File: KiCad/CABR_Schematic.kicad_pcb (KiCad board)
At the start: 2 copper layers, 23.5 x 59.1 mm, 20 parts, among them J1 Screw_Terminal_01x02, J2 0.1" Header, J3 Program Header, J4 MicroSwitch, J5 Screw_Terminal_01x02, Q1 PBSS4250X, U1 AZ1117-5.0, U2 ATtiny85-20SU

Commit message: updated PCB again
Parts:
- moved J5 3.94 mm to (145.3, 107.2)
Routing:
- net GND: track 112.9 -> 120.5 mm
- net Net-(C2-Pad1): track 57.5 -> 56.5 mm
- net Net-(C1-Pad1): track 63.1 -> 62.5 mm
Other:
- board size 23.5 x 59.1 mm -> 23.5 x 54.6 mm
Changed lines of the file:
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@@
     (thickness 1.6)
     (drawings 9)
-    (tracks 194)
+    (tracks 200)
     (zones 0)
     (modules 20)
@@
       (drillshape 0)
       (scaleselection 1)
-      (outputdirectory "C:/Users/chandler.lofland/OtherProjects/CABR/KiCad/Gerber/"))
+      (outputdirectory "G:/Projects/3D Printing/CABR/KiCad/Gerber/"))
   )
   (net 0 "")
@@
   )
   (module XT60:XT60 (layer F.Cu)
-    (at 145.415 111.125)
+    (at 145.288 107.188)
     (fp_text reference J5 (at 3.556 6.096) (layer F.SilkS)
       (effects (font (size 1 1) (thickness 0.15)))
@@
     )
   )
-  (gr_text Power (at 153.67 116.84) (layer F.SilkS)
+  (gr_text Power (at 154.432 112.776) (layer F.SilkS)
     (effects (font (size 1 1) (thickness 0.15)))
   )
-  (gr_line (start 160.655 118.745) (end 160.655 112.395) (layer Edge.Cuts) (width 0.05))
-  (gr_line (start 137.16 118.745) (end 160.655 118.745) (layer Edge.Cuts) (width 0.05))
-  (gr_line (start 137.16 112.395) (end 137.16 118.745) (layer Edge.Cuts) (width 0.05))
+  (gr_line (start 160.655 114.3) (end 160.655 112.395) (layer Edge.Cuts) (width 0.05))
+  (gr_line (start 137.16 114.3) (end 160.655 114.3) (layer Edge.Cuts) (width 0.05))
+  (gr_line (start 137.16 112.395) (end 137.16 114.3) (layer Edge.Cuts) (width 0.05))
   (gr_line (start 137.16 59.69) (end 137.16 63.5) (layer Edge.Cuts) (width 0.05))
   (gr_line (start 160.655 59.69) (end 137.16 59.69) (layer Edge.Cuts) (width 0.05))
@@
   (gr_line (start 160.655 112.395) (end 160.655 63.5) (layer Edge.Cuts) (width 0.05))
   (gr_line (start 137.16 63.5) (end 137.16 112.395) (layer Edge.Cuts) (width 0.05))
-  (segment (start 157.48 69.469) (end 153.035 65.024) (width 0.5) (layer F.Cu) (net 1))
-  (segment (start 157.48 74.55) (end 157.48 69.469) (width 0.5) (layer F.Cu) (net 1))
+  (segment (start 157.48 69.469) (end 153.035 65.024) (width 1) (layer F.Cu) (net 1))
+  (segment (start 157.48 74.55) (end 157.48 69.469) (width 1) (layer F.Cu) (net 1))
   (via (at 157.48 76.2) (size 0.8) (drill 0.4) (layers F.Cu B.Cu) (net 1))
-  (segment (start 157.48 91.44) (end 148.844 100.076) (width 0.5) (layer B.Cu) (net 1))
-  (segment (start 157.48 76.2) (end 157.48 91.44) (width 0.5) (layer B.Cu) (net 1))
-  (segment (start 157.48 74.55) (end 157.48 76.2) (width 0.5) (layer F.Cu) (net 1))
+  (segment (start 157.48 91.44) (end 148.844 100.076) (width 1) (layer B.Cu) (net 1))
+  (segment (start 157.48 76.2) (end 157.48 91.44) (width 1) (layer B.Cu) (net 1))
+  (segment (start 157.48 74.55) (end 157.48 76.2) (width 1) (layer F.Cu) (net 1))
   (via (at 148.844 100.076) (size 0.8) (drill 0.4) (layers F.Cu B.Cu) (net 1))
   (segment (start 146.089 100.076) (end 146.075 100.09) (width 0.5) (layer F.Cu) (net 1))
-  (segment (start 156.337 70.612) (end 157.48 69.469) (width 0.5) (layer F.Cu) (net 1))
-  (segment (start 154.304 70.612) (end 156.337 70.612) (width 0.5) (layer F.Cu) (net 1))
+  (segment (start 156.337 70.612) (end 157.48 69.469) (width 1) (layer F.Cu) (net 1))
+  (segment (start 154.304 70.612) (end 156.337 70.612) (width 1) (layer F.Cu) (net 1))
   (segment (start 145.6595 100.5055) (end 146.075 100.09) (width 0.25) (layer F.Cu) (net 1))
   (segment (start 143.256 100.5055) (end 145.6595 100.5055) (width 0.25) (layer F.Cu) (net 1))
-  (segment (start 145.415 102.6645) (end 143.256 100.5055) (width 0.5) (layer F.Cu) (net 1))
-  (segment (start 145.415 111.125) (end 145.415 102.6645) (width 0.5) (layer F.Cu) (net 1))
-  (segment (start 146.2555 102.6645) (end 148.844 100.076) (width 0.5) (layer F.Cu) (net 1))
-  (segment (start 145.415 102.6645) (end 146.2555 102.6645) (width 0.5) (layer F.Cu) (net 1))
+  (segment (start 146.2555 102.6645) (end 148.844 100.076) (width 1) (layer F.Cu) (net 1))
+  (segment (start 145.415 102.6645) (end 146.2555 102.6645) (width 1) (layer F.Cu) (net 1))
+  (segment (start 145.288 102.5375) (end 144.81925 102.06875) (width 0.25) (layer F.Cu) (net 1))
+  (segment (start 145.415 102.6645) (end 144.81925 102.06875) (width 1) (layer F.Cu) (net 1))
+  (segment (start 144.81925 102.06875) (end 143.256 100.5055) (width 1) (layer F.Cu) (net 1))
+  (segment (start 145.288 107.188) (end 145.288 106.68) (width 1) (layer F.Cu) (net 1))
+  (segment (start 147.828 104.14) (end 146.3525 102.6645) (width 1) (layer F.Cu) (net 1))
+  (segment (start 146.3525 102.6645) (end 145.415 102.6645) (width 1) (layer F.Cu) (net 1))
+  (segment (start 145.288 106.68) (end 147.828 104.14) (width 1) (layer F.Cu) (net 1))
   (segment (start 144.2075 95.49) (end 146.075 95.49) (width 0.25) (layer F.Cu) (net 2))
   (segment (start 143.256 96.4415) (end 144.2075 95.49) (width 0.25) (layer F.Cu) (net 2))
@@
   (segment (start 145.542 86.614) (end 145.542 84.488) (width 0.25) (layer F.Cu) (net 2))
   (via (at 150.876 72.39) (size 0.8) (drill 0.4) (layers F.Cu B.Cu) (net 2))
-  (segment (start 143.002 72.39) (end 138.938 76.454) (width 0.5) (layer B.Cu) (net 2))
-  (segment (start 150.876 72.39) (end 143.002 72.39) (width 0.5) (layer B.Cu) (net 2))
-  (segment (start 138.938 76.454) (end 138.938 98.355002) (width 0.5) (layer B.Cu) (net 2))
-  (segment (start 138.938 98.355002) (end 148.707999 108.125001) (width 0.5) (layer B.Cu) (net 2))
-  (segment (start 148.707999 108.125001) (end 149.915001 108.125001) (width 0.5) (layer B.Cu) (net 2))
-  (segment (start 149.915001 108.125001) (end 152.915 111.125) (width 0.5) (layer B.Cu) (net 2))
+  (segment (start 143.002 72.39) (end 138.938 76.454) (width 1) (layer B.Cu) (net 2))
+  (segment (start 150.876 72.39) (end 143.002 72.39) (width 1) (layer B.Cu) (net 2))
+  (segment (start 138.938 76.454) (end 138.938 98.355002) (width 1) (layer B.Cu) (net 2))
   (segment (start 150.92 72.434) (end 150.876 72.39) (width 0.5) (layer F.Cu) (net 2))
-  (segment (start 150.92 74.065) (end 150.92 72.434) (width 0.5) (layer F.Cu) (net 2))
+  (segment (start 150.92 74.065) (end 150.92 72.434) (width 1) (layer F.Cu) (net 2))
   (segment (start 143.256 98.6305) (end 143.256 96.4415) (width 0.25) (layer F.Cu) (net 2))
   (via (at 140.716 98.044) (size 0.8) (drill 0.4) (layers F.Cu B.Cu) (net 2))
@@
   (segment (start 156.8935 97.028) (end 156.8935 92.456) (width 0.25) (layer F.Cu) (net 2))
   (segment (start 155.194 98.7275) (end 156.8935 97.028) (width 0.25) (layer F.Cu) (net 2))
+  (segment (start 138.938 107.95) (end 138.938 98.355002) (width 1) (layer B.Cu) (net 2))
+  (segment (start 148.216 111.76) (end 142.748 111.76) (width 1) (layer B.Cu) (net 2))
+  (segment (start 152.788 107.188) (end 148.216 111.76) (width 1) (layer B.Cu) (net 2))
+  (segment (start 142.748 111.76) (end 138.938 107.95) (width 1) (layer B.Cu) (net 2))
   (segment (start 141.605 86.825) (end 141.605 85.725) (width 0.25) (layer F.Cu) (net 3))
   (segment (start 144.409999 89.629999) (end 141.605 86.825) (width 0.25) (layer F.Cu) (net 3))
   (segment (start 148.049999 89.629999) (end 144.409999 89.629999) (width 0.25) (layer F.Cu) (net 3))
   (segment (start 149.225 90.805) (end 148.049999 89.629999) (width 0.25) (layer F.Cu) (net 3))
-  (segment (start 140.505 85.725) (end 138.43 83.65) (width 0.25) (layer F.Cu) (net 3))
-  (segment (start 141.605 85.725) (end 140.505 85.725) (width 0.25) (layer F.Cu) (net 3))
-  (segment (start 138.43 83.65) (end 138.43 78.74) (width 0.25) (layer F.Cu) (net 3))
-  (segment (start 139.954 77.216) (end 141.224 77.216) (width 0.25) (layer F.Cu) (net 3))
-  (segment (start 138.43 78.74) (end 139.954 77.216) (width 0.25) (layer F.Cu) (net 3))
   (segment (start 152.375 97.79) (end 146.075 97.79) (width 0.25) (layer F.Cu) (net 3))
   (via (at 156.718 82.46) (size 0.8) (drill 0.4) (layers F.Cu B.Cu) (net 3))
@@
   (segment (start 155.194 96.8525) (end 155.194 95.504) (width 0.25) (layer F.Cu) (net 3))
   (segment (start 155.194 95.504) (end 154.686 94.996) (width 0.25) (layer F.Cu) (net 3))
+  (segment (start 139.954 77.216) (end 141.224 77.216) (width 0.25) (layer F.Cu) (net 3))
+  (segment (start 139.7 77.47) (end 139.954 77.216) (width 0.25) (layer F.Cu) (net 3))
+  (segment (start 139.7 84.92) (end 139.7 77.47) (width 0.25) (layer F.Cu) (net 3))
+  (segment (start 141.605 85.725) (end 140.505 85.725) (width 0.25) (layer F.Cu) (net 3))
+  (segment (start 140.505 85.725) (end 139.7 84.92) (width 0.25) (layer F.Cu) (net 3))
   (segment (start 143.256 93.315) (end 143.256 94.5665) (width 0.25) (layer F.Cu) (net 4))
   (segment (start 142.24 92.299) (end 143.256 93.315) (width 0.25) (layer F.Cu) (net 4))
@@
   (segment (start 145.161 83.185) (end 145.575 83.185) (width 0.25) (layer F.Cu) (net 5))
   (segment (start 144.018 84.328) (end 145.161 83.185) (width 0.25) (layer F.Cu) (net 5))
-  (segment (start 145.535 65.024) (end 149.352 68.841) (width 0.5) (layer F.Cu) (net 6))
-  (segment (start 149.352 68.841) (end 149.352 74.2505) (width 0.5) (layer F.Cu) (net 6))
-  (segment (start 149.352 74.2505) (end 150.6665 75.565) (width 0.5) (layer F.Cu) (net 6))
+  (segment (start 145.535 65.024) (end 149.352 68.841) (width 1) (layer F.Cu) (net 6))
+  (segment (start 149.352 68.841) (end 149.352 74.2505) (width 1) (layer F.Cu) (net 6))
+  (segment (start 149.352 74.2505) (end 150.6665 75.565) (width 1) (layer F.Cu) (net 6))
   (segment (start 150.6665 75.565) (end 151.0665 75.565) (width 0.5) (layer F.Cu) (net 6))
   (segment (start 155.067 75.587) (end 155.067 75.565) (width 0.5) (layer F.Cu) (net 6))
   (segment (start 151.0665 75.565) (end 155.067 75.565) (width 0.25) (layer F.Cu) (net 6))
   (segment (start 151.004 70.462) (end 151.004 70.612) (width 0.25) (layer F.Cu) (net 6))
-  (segment (start 149.383 68.841) (end 151.004 70.462) (width 0.5) (layer F.Cu) (net 6))
+  (segment (start 149.383 68.841) (end 151.004 70.462) (width 1) (layer F.Cu) (net 6))
   (segment (start 149.352 68.841) (end 149.383 68.841) (width 0.25) (layer F.Cu) (net 6))
   (via (at 151.13 85.725) (size 0.8) (drill 0.4) (layers F.Cu B.Cu) (net 7))

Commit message: edited step file
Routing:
- net Net-(C2-Pad1): track 56.5 -> 58.0 mm
- net Net-(J4-Pad2): track 26.7 -> 27.9 mm
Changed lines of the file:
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@@
     (thickness 1.6)
     (drawings 9)
-    (tracks 200)
+    (tracks 199)
     (zones 0)
     (modules 20)
@@
   (segment (start 156.8935 92.456) (end 158.242 91.1075) (width 0.25) (layer F.Cu) (net 2))
   (via (at 147.315347 84.840653) (size 0.8) (drill 0.4) (layers F.Cu B.Cu) (net 2))
-  (segment (start 146.075 91.415) (end 146.685 90.805) (width 0.25) (layer F.Cu) (net 2))
-  (segment (start 146.075 95.49) (end 146.075 91.415) (width 0.25) (layer F.Cu) (net 2))
   (via (at 144.272 90.678) (size 0.8) (drill 0.4) (layers F.Cu B.Cu) (net 2))
   (segment (start 146.685 90.805) (end 144.399 90.805) (width 0.25) (layer F.Cu) (net 2))
@@
   (segment (start 138.938 98.355002) (end 139.249002 98.044) (width 0.25) (layer B.Cu) (net 2))
   (segment (start 141.281685 98.044) (end 140.716 98.044) (width 0.25) (layer F.Cu) (net 2))
-  (segment (start 156.8935 97.028) (end 156.8935 92.456) (width 0.25) (layer F.Cu) (net 2))
-  (segment (start 155.194 98.7275) (end 156.8935 97.028) (width 0.25) (layer F.Cu) (net 2))
   (segment (start 138.938 107.95) (end 138.938 98.355002) (width 1) (layer B.Cu) (net 2))
   (segment (start 148.216 111.76) (end 142.748 111.76) (width 1) (layer B.Cu) (net 2))
   (segment (start 152.788 107.188) (end 148.216 111.76) (width 1) (layer B.Cu) (net 2))
   (segment (start 142.748 111.76) (end 138.938 107.95) (width 1) (layer B.Cu) (net 2))
+  (segment (start 146.685 92.964) (end 146.685 90.805) (width 0.25) (layer F.Cu) (net 2))
+  (segment (start 146.685 93.218) (end 146.685 92.964) (width 0.25) (layer F.Cu) (net 2))
+  (segment (start 146.075 95.49) (end 146.075 93.828) (width 0.25) (layer F.Cu) (net 2))
+  (segment (start 146.075 93.828) (end 146.685 93.218) (width 0.25) (layer F.Cu) (net 2))
+  (segment (start 155.194 98.7275) (end 157.449737 96.471763) (width 0.25) (layer F.Cu) (net 2))
+  (segment (start 157.449737 96.471763) (end 157.449737 93.012237) (width 0.25) (layer F.Cu) (net 2))
+  (segment (start 157.449737 93.012237) (end 156.8935 92.456) (width 0.25) (layer F.Cu) (net 2))
   (segment (start 141.605 86.825) (end 141.605 85.725) (width 0.25) (layer F.Cu) (net 3))
   (segment (start 144.409999 89.629999) (end 141.605 86.825) (width 0.25) (layer F.Cu) (net 3))
@@
   (segment (start 149.225 90.805) (end 148.049999 89.629999) (width 0.25) (layer F.Cu) (net 3))
   (segment (start 152.375 97.79) (end 146.075 97.79) (width 0.25) (layer F.Cu) (net 3))
-  (via (at 156.718 82.46) (size 0.8) (drill 0.4) (layers F.Cu B.Cu) (net 3))
-  (segment (start 156.318001 82.859999) (end 156.318001 86.505999) (width 0.25) (layer B.Cu) (net 3))
-  (segment (start 156.718 82.46) (end 156.318001 82.859999) (width 0.25) (layer B.Cu) (net 3))
-  (via (at 153.416 89.408) (size 0.8) (drill 0.4) (layers F.Cu B.Cu) (net 3))
-  (segment (start 156.318001 86.505999) (end 153.416 89.408) (width 0.25) (layer B.Cu) (net 3))
-  (segment (start 150.074999 89.955001) (end 149.225 90.805) (width 0.25) (layer F.Cu) (net 3))
-  (segment (start 150.400001 89.629999) (end 150.074999 89.955001) (width 0.25) (layer F.Cu) (net 3))
-  (segment (start 152.628316 89.629999) (end 150.400001 89.629999) (width 0.25) (layer F.Cu) (net 3))
-  (segment (start 152.850315 89.408) (end 152.628316 89.629999) (width 0.25) (layer F.Cu) (net 3))
-  (segment (start 153.416 89.408) (end 152.850315 89.408) (width 0.25) (layer F.Cu) (net 3))
-  (segment (start 156.628 82.55) (end 156.718 82.46) (width 0.25) (layer F.Cu) (net 3))
-  (segment (start 157.226 82.55) (end 156.628 82.55) (width 0.25) (layer F.Cu) (net 3))
-  (segment (start 157.7825 81.28) (end 157.7825 81.9935) (width 0.25) (layer F.Cu) (net 3))
-  (segment (start 157.7825 81.9935) (end 157.226 82.55) (width 0.25) (layer F.Cu) (net 3))
   (segment (start 154.2565 97.79) (end 155.194 96.8525) (width 0.25) (layer F.Cu) (net 3))
   (segment (start 152.375 97.79) (end 154.2565 97.79) (width 0.25) (layer F.Cu) (net 3))
+  (segment (start 139.954 77.216) (end 141.224 77.216) (width 0.25) (layer F.Cu) (net 3))
+  (segment (start 139.7 77.47) (end 139.954 77.216) (width 0.25) (layer F.Cu) (net 3))
+  (segment (start 139.7 84.92) (end 139.7 77.47) (width 0.25) (layer F.Cu) (net 3))
+  (segment (start 141.605 85.725) (end 140.505 85.725) (width 0.25) (layer F.Cu) (net 3))
+  (segment (start 140.505 85.725) (end 139.7 84.92) (width 0.25) (layer F.Cu) (net 3))
   (segment (start 149.225 92.007081) (end 149.225 90.805) (width 0.25) (layer F.Cu) (net 3))
   (segment (start 152.213919 94.996) (end 149.225 92.007081) (width 0.25) (layer F.Cu) (net 3))
@@
   (segment (start 155.194 96.8525) (end 155.194 95.504) (width 0.25) (layer F.Cu) (net 3))
   (segment (start 155.194 95.504) (end 154.686 94.996) (width 0.25) (layer F.Cu) (net 3))
-  (segment (start 139.954 77.216) (end 141.224 77.216) (width 0.25) (layer F.Cu) (net 3))
-  (segment (start 139.7 77.47) (end 139.954 77.216) (width 0.25) (layer F.Cu) (net 3))
-  (segment (start 139.7 84.92) (end 139.7 77.47) (width 0.25) (layer F.Cu) (net 3))
-  (segment (start 141.605 85.725) (end 140.505 85.725) (width 0.25) (layer F.Cu) (net 3))
-  (segment (start 140.505 85.725) (end 139.7 84.92) (width 0.25) (layer F.Cu) (net 3))
+  (via (at 159.258 82.804) (size 0.8) (drill 0.4) (layers F.Cu B.Cu) (net 3))
+  (segment (start 159.258 82.7555) (end 157.7825 81.28) (width 0.25) (layer F.Cu) (net 3))
+  (segment (start 159.258 82.804) (end 159.258 82.7555) (width 0.25) (layer F.Cu) (net 3))
+  (segment (start 159.258 82.804) (end 159.258 91.9065) (width 0.25) (layer B.Cu) (net 3))
+  (segment (start 156.568499 94.596001) (end 156.1685 94.996) (width 0.25) (layer B.Cu) (net 3))
+  (segment (start 159.258 91.9065) (end 156.568499 94.596001) (width 0.25) (layer B.Cu) (net 3))
+  (via (at 156.1685 94.996) (size 0.8) (drill 0.4) (layers F.Cu B.Cu) (net 3))
+  (segment (start 155.9145 95.25) (end 156.1685 94.996) (width 0.25) (layer F.Cu) (net 3))
+  (segment (start 155.194 95.504) (end 155.448 95.25) (width 0.25) (layer F.Cu) (net 3))
+  (segment (start 155.448 95.25) (end 155.9145 95.25) (width 0.25) (layer F.Cu) (net 3))
   (segment (start 143.256 93.315) (end 143.256 94.5665) (width 0.25) (layer F.Cu) (net 4))
   (segment (start 142.24 92.299) (end 143.256 93.315) (width 0.25) (layer F.Cu) (net 4))
@@
   (segment (start 142.875 81.915) (end 143.891 81.915) (width 0.25) (layer F.Cu) (net 11))
   (segment (start 143.891 81.915) (end 145.575 81.915) (width 0.25) (layer F.Cu) (net 11))
-  (segment (start 140.429999 88.163001) (end 145.230998 92.964) (width 0.25) (layer B.Cu) (net 11))
-  (segment (start 141.605 83.185) (end 140.429999 84.360001) (width 0.25) (layer B.Cu) (net 11))
-  (segment (start 140.429999 84.360001) (end 140.429999 88.163001) (width 0.25) (layer B.Cu) (net 11))
   (via (at 151.638 92.964) (size 0.8) (drill 0.4) (layers F.Cu B.Cu) (net 11))
-  (segment (start 145.230998 92.964) (end 151.638 92.964) (width 0.25) (layer B.Cu) (net 11))
   (segment (start 151.638 92.964) (end 153.416 92.964) (width 0.25) (layer F.Cu) (net 11))
   (segment (start 153.924 92.456) (end 155.0185 92.456) (width 0.25) (layer F.Cu) (net 11))
   (segment (start 153.416 92.964) (end 153.924 92.456) (width 0.25) (layer F.Cu) (net 11))
+  (segment (start 143.51 92.964) (end 151.638 92.964) (width 0.25) (layer B.Cu) (net 11))
+  (segment (start 140.208 89.662) (end 143.51 92.964) (width 0.25) (layer B.Cu) (net 11))
+  (segment (start 141.605 83.185) (end 140.208 84.582) (width 0.25) (layer B.Cu) (net 11))
+  (segment (start 140.208 84.582) (end 140.208 89.662) (width 0.25) (layer B.Cu) (net 11))
   (segment (start 149.92 77.065) (end 150.92 77.065) (width 0.25) (layer F.Cu) (net 12))
   (segment (start 148.2575 75.4025) (end 149.92 77.065) (width 0.25) (layer F.Cu) (net 12))

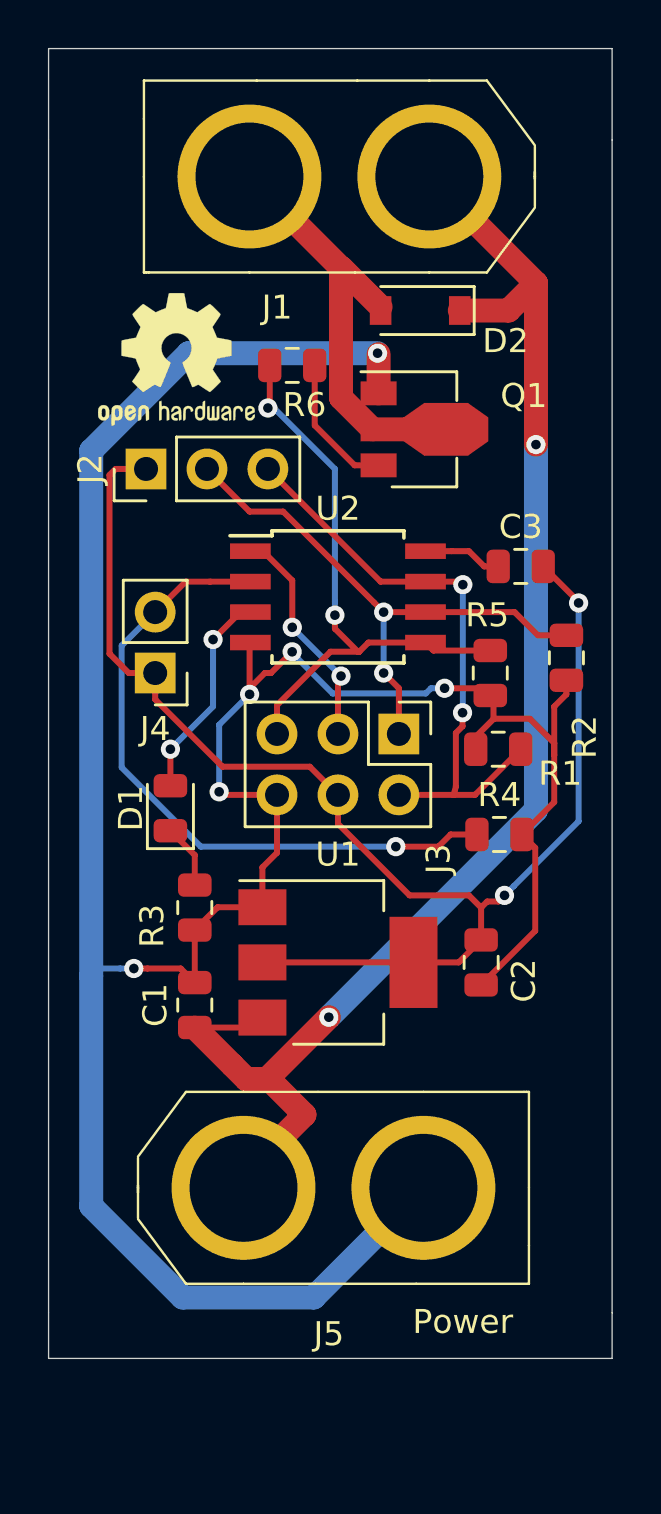
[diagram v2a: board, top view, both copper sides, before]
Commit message: fixed issue with boardfire
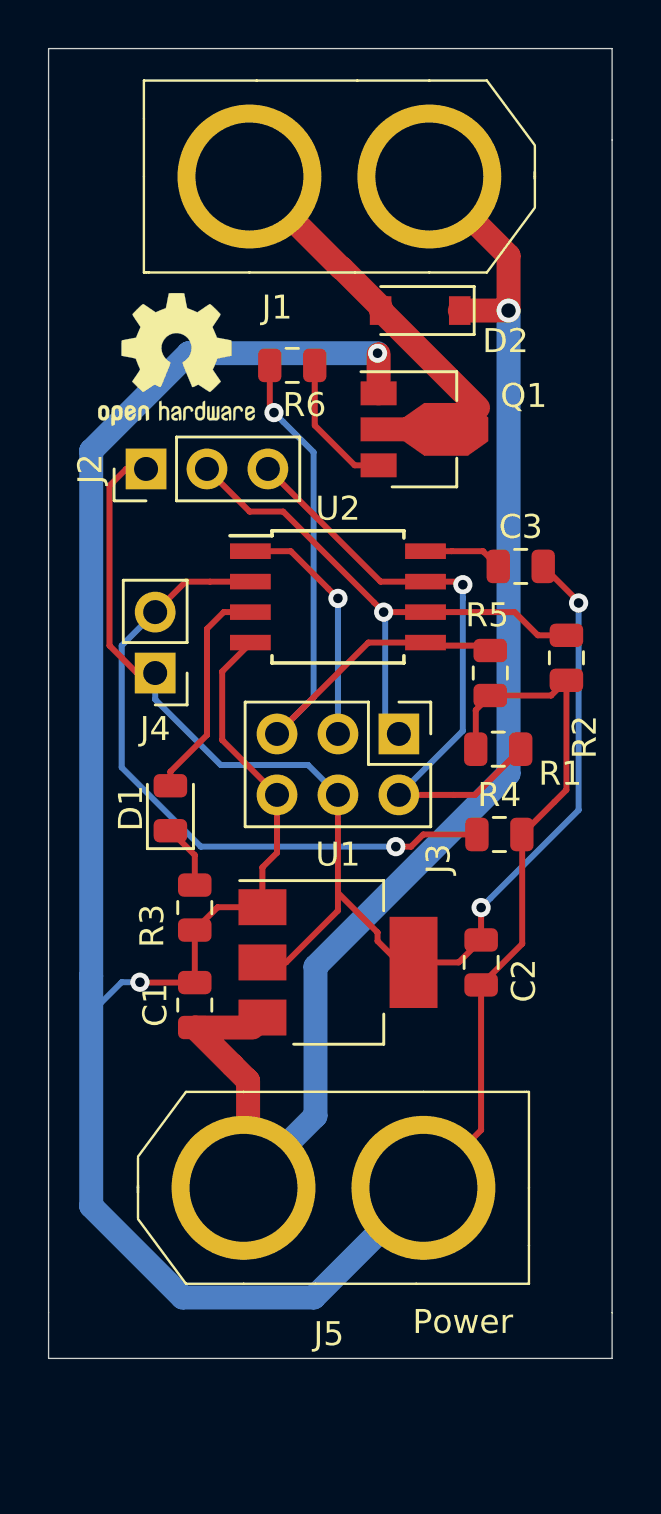
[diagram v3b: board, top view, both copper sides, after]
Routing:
- net GND: track 121.0 -> 118.2 mm, vias 6 -> 2
- net Net-(J3-Pad5): track 25.0 -> 27.4 mm, vias 2 -> 1
- net Net-(C2-Pad1): track 58.0 -> 55.7 mm
- net Net-(D2-Pad2): track 19.6 -> 18.5 mm
- net Net-(C1-Pad1): track 62.5 -> 61.5 mm, vias 2 -> 1
- net Net-(J2-Pad3): track 24.9 -> 25.9 mm, vias 2 -> 1
- net Net-(J3-Pad3): track 9.54 -> 10.1 mm, vias 2 -> 1
- net Net-(D1-Pad2): track 8.86 -> 9.27 mm, vias 2 -> 0
- net Net-(J2-Pad2): vias 2 -> 1
